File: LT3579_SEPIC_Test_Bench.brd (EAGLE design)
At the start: 300 x 300 mm, 121 parts

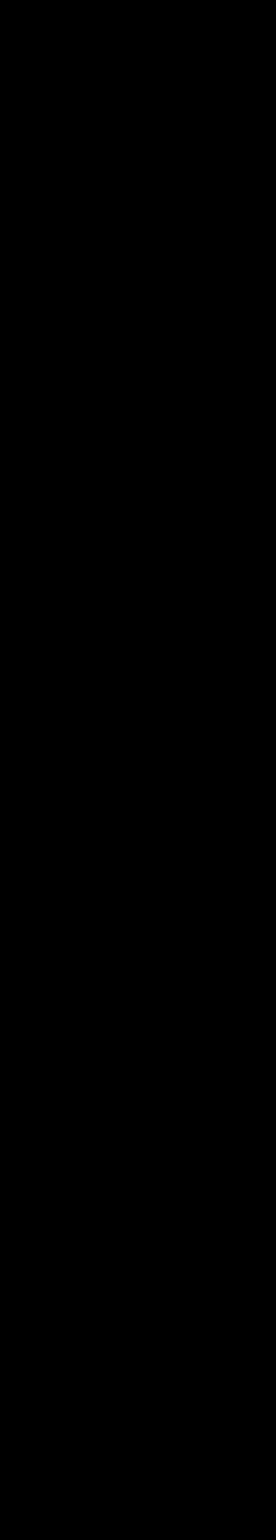
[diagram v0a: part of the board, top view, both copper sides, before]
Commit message: Added new componants to schematic and board layout
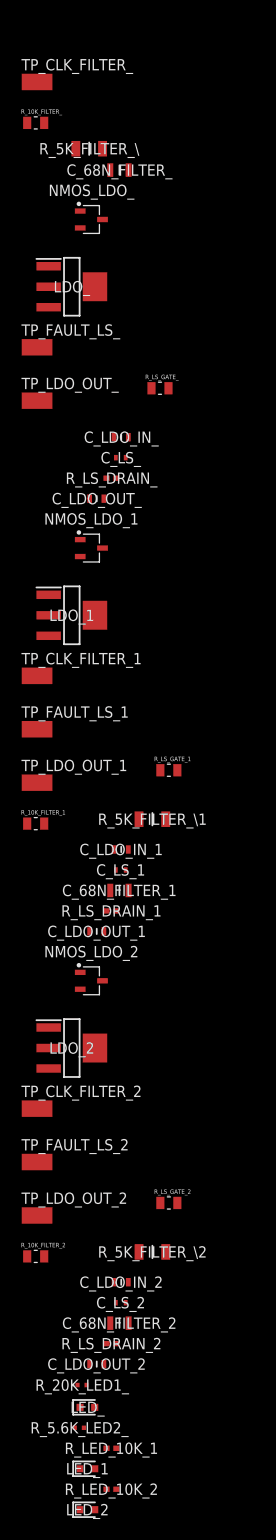
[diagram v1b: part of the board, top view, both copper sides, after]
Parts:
- added C_68N_FILTER_, C_68N_FILTER_1, C_68N_FILTER_2: CEU4J2X7R1H683K125AE, SamacSys_Parts:CAPC2013X150N
- added C_LDO_IN_, C_LDO_IN_1, C_LDO_IN_2: CGA3E1X7R1V105K080AC, SamacSys_Parts:CAPC1608X90N
- added C_LDO_OUT_, C_LDO_OUT_1, C_LDO_OUT_2: JMK107BB7475KA-T, SamacSys_Parts:CAPC1608X90N
- added C_LS_, C_LS_1, C_LS_2: CGA2B2C0G1H102J050BE, SamacSys_Parts:CAPC1005X55N
- added LDO_, LDO_1, LDO_2: LDL1117S33R, SamacSys_Parts:SOT230P700X180-4N
- added LED_, LED_1, LED_2: APTD1608LCGCK, SamacSys_Parts:APT1608CGCK
- added NMOS_LDO_, NMOS_LDO_1, NMOS_LDO_2: RTR025N05HZGTL, SamacSys_Parts:SOT95P280X110-3N
- added R_10K_FILTER_, R_10K_FILTER_1, R_10K_FILTER_2: AC0805DR-0710KL, AC0805DR-0710KL:RESC2012X60N
- added R_20K_LED1_: ERJ-2RKF2002X, SamacSys_Parts:ERJ2R_(0402)
- added R_5.6K_LED2_: ERA-2ARB562X, SamacSys_Parts:ERA2AED122X
- added R_5K_FILTER_\, R_5K_FILTER_\1, R_5K_FILTER_\2: RT1206BRD075KL, SamacSys_Parts:RESC3116X65N
- added R_LED_10K_1, R_LED_10K_2, R_LS_DRAIN_, R_LS_DRAIN_1, R_LS_DRAIN_2: MCS0402MD1002DE000, SamacSys_Parts:RESC1005X37N
- added R_LS_GATE_, R_LS_GATE_1, R_LS_GATE_2: AT0805FRE07100KL, AT0805FRE07100KL:RESC2012X60N
- added TP_CLK_FILTER_, TP_CLK_FILTER_1, TP_CLK_FILTER_2, TP_FAULT_LS_, TP_FAULT_LS_1, TP_FAULT_LS_2, TP_LDO_OUT_, TP_LDO_OUT_1, TP_LDO_OUT_2: S1751-46R, S1751-46R:S1751-46R_
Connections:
- new net CLK_FILTER_OUT_: 12P_OUTPUT_CONNECTOR1.6, C_68N_FILTER_.1, R_10K_FILTER_.2, R_5K_FILTER_\.1, TP_CLK_FILTER_.1
- new net CLK_FILTER_OUT_1: 12P_OUTPUT_CONNECTOR1.4, C_68N_FILTER_1.1, R_10K_FILTER_1.2, R_5K_FILTER_\1.1, TP_CLK_FILTER_1.1
- new net CLK_FILTER_OUT_2: 12P_OUTPUT_CONNECTOR1.2, C_68N_FILTER_2.1, R_10K_FILTER_2.2, R_5K_FILTER_\2.1, TP_CLK_FILTER_2.1
- new net FAULT_LS_OUT_: 12P_OUTPUT_CONNECTOR1.5, C_LS_.1, NMOS_LDO_.3, R_LS_DRAIN_.1, TP_FAULT_LS_.1
- new net FAULT_LS_OUT_1: 12P_OUTPUT_CONNECTOR1.3, C_LS_1.1, NMOS_LDO_1.3, R_LS_DRAIN_1.1, TP_FAULT_LS_1.1
- new net FAULT_LS_OUT_2: 12P_OUTPUT_CONNECTOR1.1, C_LS_2.1, NMOS_LDO_2.3, R_LS_DRAIN_2.1, TP_FAULT_LS_2.1
- new net LDO_OUT_: C_LDO_OUT_.1, LDO_.2, LDO_.4, R_LS_DRAIN_.2, TP_LDO_OUT_.1
- new net LDO_OUT_1: C_LDO_OUT_1.1, LDO_1.2, LDO_1.4, R_LS_DRAIN_1.2, TP_LDO_OUT_1.1
- new net LDO_OUT_2: C_LDO_OUT_2.1, LDO_2.2, LDO_2.4, R_LS_DRAIN_2.2, TP_LDO_OUT_2.1
- new net N$10: NMOS_LDO_1.1, R_LS_GATE_1.2
- new net N$11: LED_1.1, R_LED_10K_1.2
- new net N$12: R_20K_LED1_.1, R_5.6K_LED2_.1
- new net N$14: NMOS_LDO_2.1, R_LS_GATE_2.2
- new net N$15: LED_.1, R_5.6K_LED2_.2
- new net N$16: LED_2.1, R_LED_10K_2.2
- new net N$8: NMOS_LDO_.1, R_LS_GATE_.2
- net 0: now also C_68N_FILTER_.2, C_68N_FILTER_1.2, C_68N_FILTER_2.2, C_LDO_IN_.2, C_LDO_IN_1.2, C_LDO_IN_2.2, C_LDO_OUT_.2, C_LDO_OUT_1.2, C_LDO_OUT_2.2, C_LS_.2, C_LS_1.2, C_LS_2.2, LED_.2, LED_1.2, LED_2.2, NMOS_LDO_.2, NMOS_LDO_1.2, NMOS_LDO_2.2, R_5K_FILTER_\.2, R_5K_FILTER_\1.2, R_5K_FILTER_\2.2
- net CLK_: now also R_10K_FILTER_.1; no longer 12P_OUTPUT_CONNECTOR1.6
- net CLK_1: now also R_10K_FILTER_1.1; no longer 12P_OUTPUT_CONNECTOR1.4
- net CLK_2: now also R_10K_FILTER_2.1; no longer 12P_OUTPUT_CONNECTOR1.2
- net FAULT_: now also R_LS_GATE_.1; no longer 12P_OUTPUT_CONNECTOR1.5
- net FAULT_1: now also R_LS_GATE_1.1; no longer 12P_OUTPUT_CONNECTOR1.3
- net FAULT_2: now also R_LS_GATE_2.1; no longer 12P_OUTPUT_CONNECTOR1.1
- net GND: now also LDO_.1, LDO_1.1, LDO_2.1
- net VIN: now also C_LDO_IN_.1, C_LDO_IN_1.1, C_LDO_IN_2.1, LDO_.3, LDO_1.3, LDO_2.3
- net VOUT_: now also R_20K_LED1_.2
- net VOUT_1: now also R_LED_10K_1.1
- net VOUT_2: now also R_LED_10K_2.1

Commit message: Modified Board File
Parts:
- moved R_5.6K_LED2_ 269.7 mm to (123.4, 99.4), turned to 270 degrees
- moved R_20K_LED1_ 269.0 mm to (123.4, 103.5), turned to 90 degrees
- moved LED_ 265.3 mm to (120.3, 99.3), turned to 90 degrees
- moved LED_1 226.6 mm to (117.8, 39.6), turned to 270 degrees
- moved R_LED_10K_1 222.4 mm to (115.5, 41.5), turned to 270 degrees
- moved LED_2 198.6 mm to (119.9, -17.7), turned to 270 degrees
- moved R_LED_10K_2 193.7 mm to (117.5, -16.3), turned to 270 degrees
- moved TP_CLK_FILTER_1 181.0 mm to (115.1, 23.5)
- moved TP_CLK_FILTER_ 180.1 mm to (115.5, 84.5)
- moved C_68N_FILTER_1 179.9 mm to (114.5, 27.0)
- moved R_10K_FILTER_1 179.4 mm to (104.8, 33.8)
- moved R_10K_FILTER_ 178.5 mm to (110.4, 93.4)
- moved R_5K_FILTER_\ 178.3 mm to (116.2, 90.6)
- moved R_10K_FILTER_2 176.9 mm to (106.1, -25.4)
- moved C_68N_FILTER_ 174.5 mm to (115.5, 88.3)
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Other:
- board size 300 x 300 mm -> 177.6 x 301.4 mm

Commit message: Modified Board Layout
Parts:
- moved R_SHUNT_GND_2 36.8 mm to (59.4, -50.8)
- moved TP_IN_1 36.5 mm to (87.7, 7.64)
- moved TP_GND_2 36.4 mm to (61.3, -45.6)
- moved TP_CH_GND_2 35.7 mm to (57.5, -45.1)
- moved C_IN_1_2 29.9 mm to (84.1, -69.6)
- moved C_LS_2 29.9 mm to (72.3, -59.2)
- moved L1L2_2 29.9 mm to (93.7, -67.8)
- moved R_T_2 29.9 mm to (99.8, -56.9)
- moved TP_CLK_FILTER_2 29.9 mm to (102.8, -62.5)
- moved TP_FB_2 29.9 mm to (84.7, -57.9)
- moved TP_SHDN_2 29.9 mm to (105.1, -54.3)
- moved TP_SS_2 29.9 mm to (99.3, -49.2)
- moved C_1_2 29.9 mm to (89.0, -59.2)
- moved C_68N_FILTER_2 29.9 mm to (104.8, -60.1)
- moved C_F_2 29.9 mm to (83.9, -48.2)
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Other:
- board size 177.6 x 301.4 mm -> 567.8 x 300.7 mm

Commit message: Modified Board
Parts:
- moved LDO_2 142.2 mm to (7.70, 57.4)
- moved TP_RT_2 100.8 mm to (70.2, 37.1), flipped to the bottom
- moved C_F_2 98.9 mm to (35.5, 38.0)
- moved C_LDO_OUT_2 98.7 mm to (35.3, 20.5)
- moved TP_LDO_OUT_2 96.8 mm to (28.0, 22.2)
- moved R_T_2 96.8 mm to (66.2, 33.9), flipped to the bottom, turned to 180 degrees
- moved TP_FAULT_LS_2 96.3 mm to (28.1, 25.4)
- moved C_C_2 96.3 mm to (36.0, 34.3), turned to 180 degrees
- moved TP_FB_2 95.8 mm to (40.4, 27.0), flipped to the bottom, turned to 180 degrees
- moved R_C_2 95.5 mm to (40.4, 34.4), turned to 180 degrees
- moved TP_SS_2 95.1 mm to (66.2, 39.9), flipped to the bottom
- moved C_SS_2 94.9 mm to (66.0, 37.1), flipped to the bottom, turned to 180 degrees
- moved C_LDO_IN_2 93.5 mm to (40.0, 14.2)
- moved R_GATE_2 93.3 mm to (47.5, 33.8), flipped to the bottom, turned to 180 degrees
- moved TP_GATE_2 93.2 mm to (51.4, 33.7), flipped to the bottom
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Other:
- board size 567.8 x 300.7 mm -> 100 x 140 mm

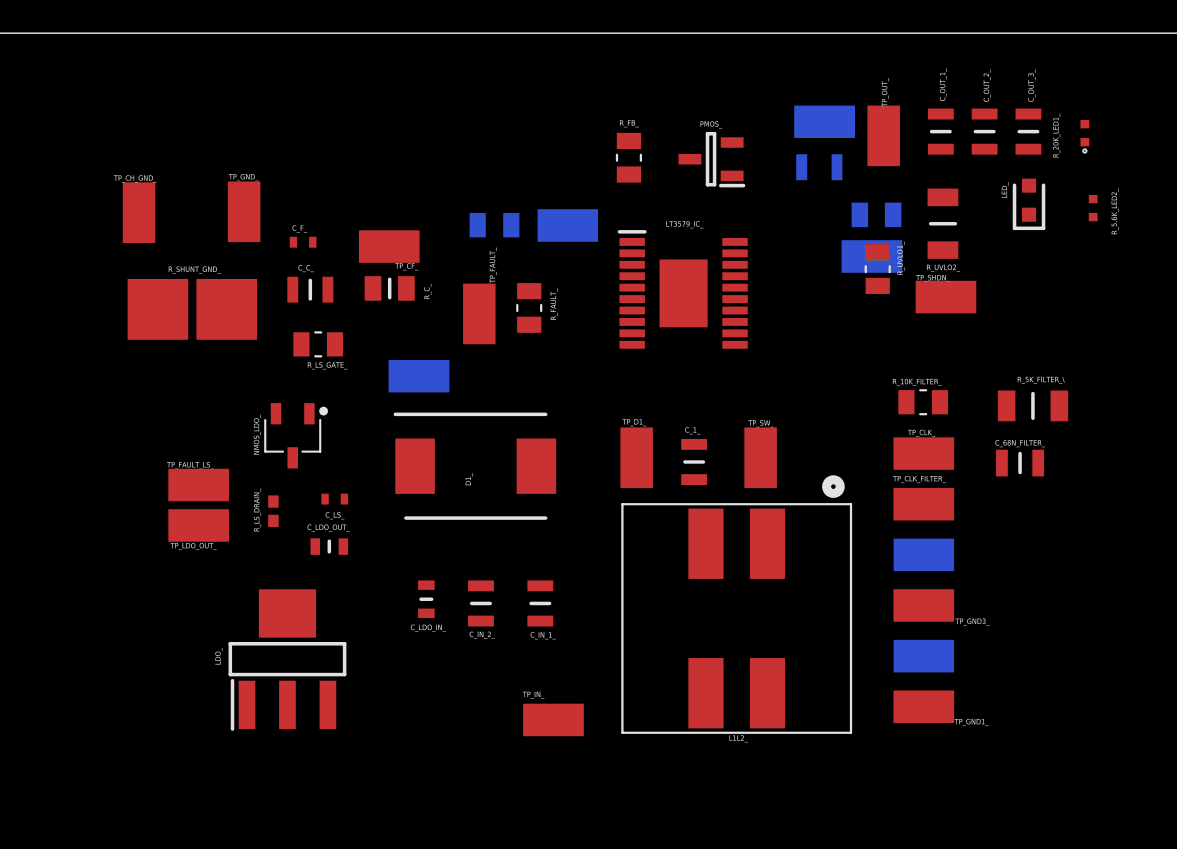
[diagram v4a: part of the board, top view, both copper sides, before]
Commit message: modified board layout
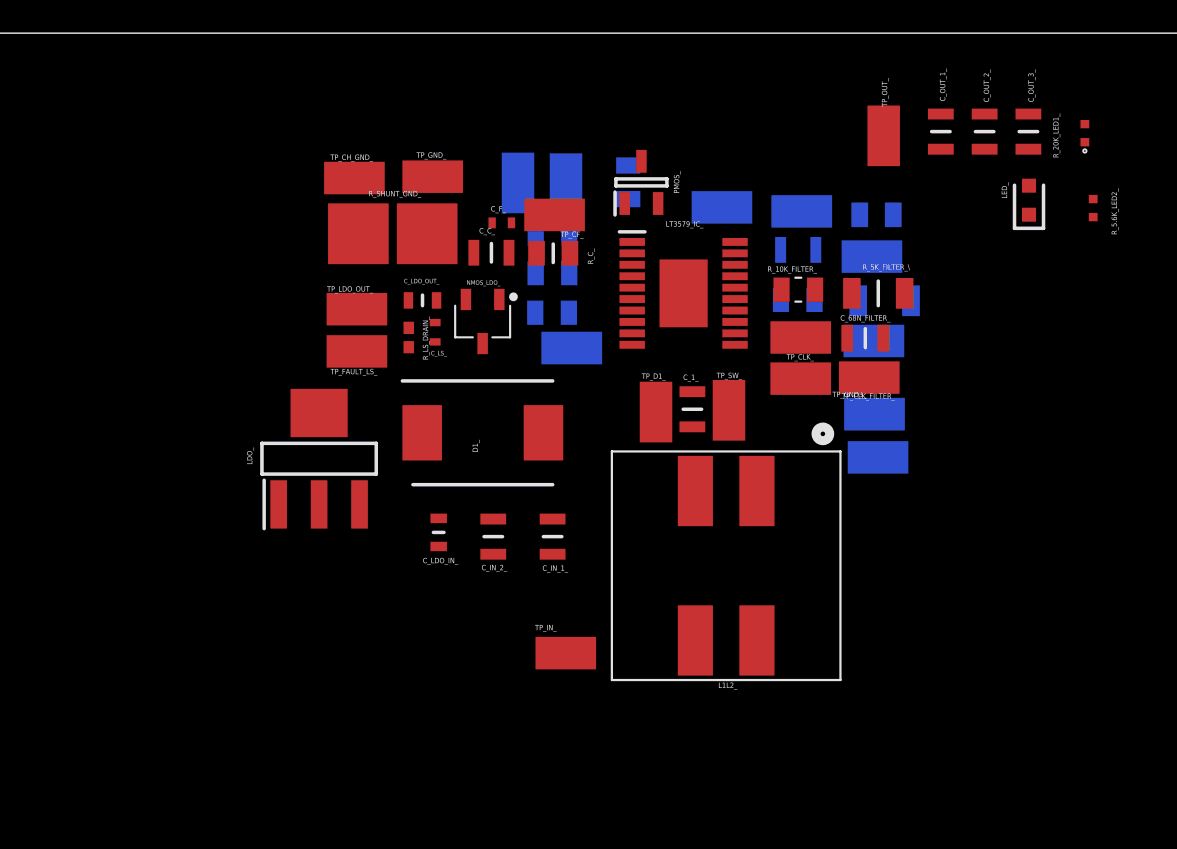
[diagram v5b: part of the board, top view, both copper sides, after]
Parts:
- moved TP_GND1_ 30.6 mm to (59.9, 130.1), flipped to the bottom
- moved TP_LDO_OUT_ 15.2 mm to (39.1, 124.3)
- moved C_LDO_OUT_ 15.0 mm to (42.9, 124.8)
- moved TP_GND3_ 14.7 mm to (64.4, 120.3)
- moved R_LS_GATE_ 13.4 mm to (50.2, 124.1), flipped to the bottom, turned to 0 degrees
- moved NMOS_LDO_ 12.6 mm to (46.3, 123.6)
- moved R_LS_DRAIN_ 12.5 mm to (42.1, 122.7), turned to 90 degrees
- moved TP_CH_GND_ 12.4 mm to (39.0, 131.8), turned to 180 degrees
- moved TP_FB_ 12.3 mm to (48.3, 131.5), turned to 270 degrees
- moved R_SHUNT_GND_ 12.2 mm to (41.2, 128.6)
- moved TP_FAULT_LS_ 11.8 mm to (39.1, 121.9)
- moved TP_GND2_ 11.6 mm to (68.8, 115.9)
- moved LDO_ 11.5 mm to (37.0, 115.8)
- moved C_F_ 11.4 mm to (47.4, 129.2)
- moved C_68N_FILTER_ 11.3 mm to (68.1, 122.7)
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
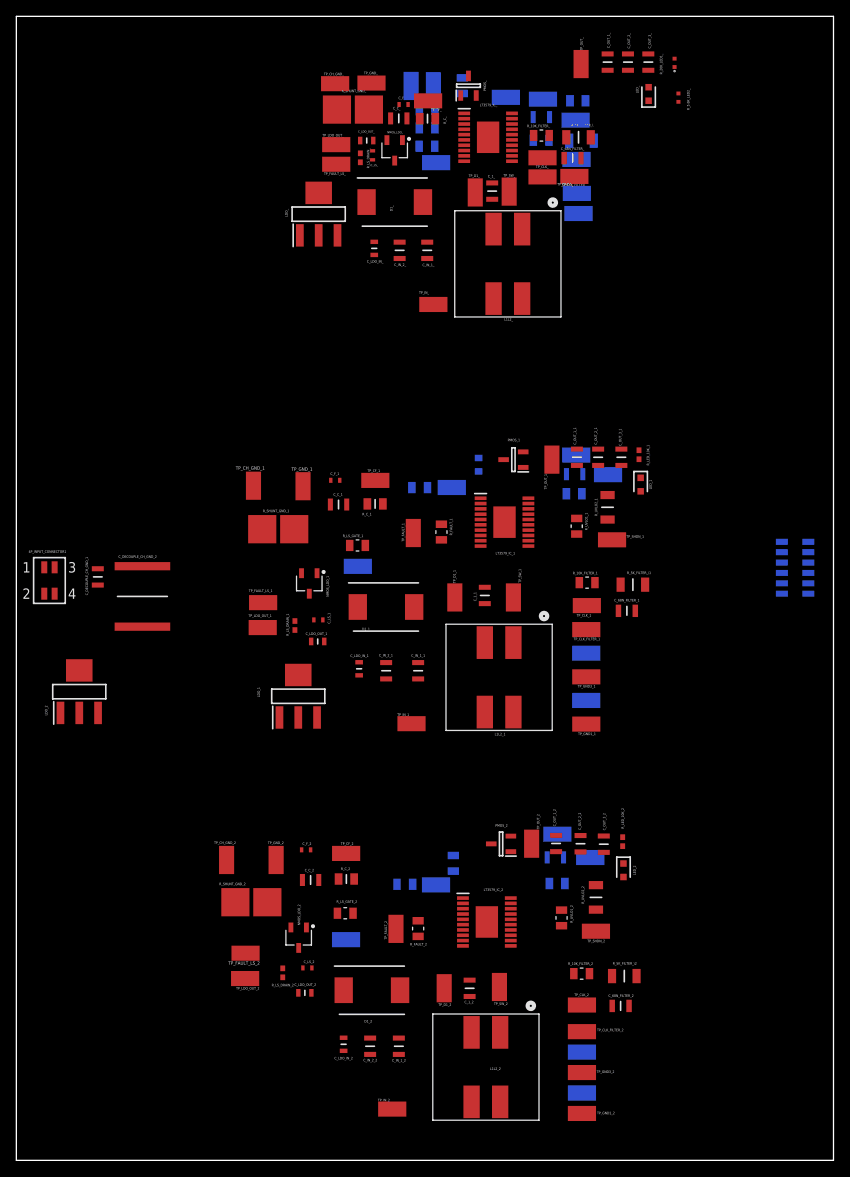
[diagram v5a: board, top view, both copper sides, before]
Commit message: Made board layout more compact. used more backside of board
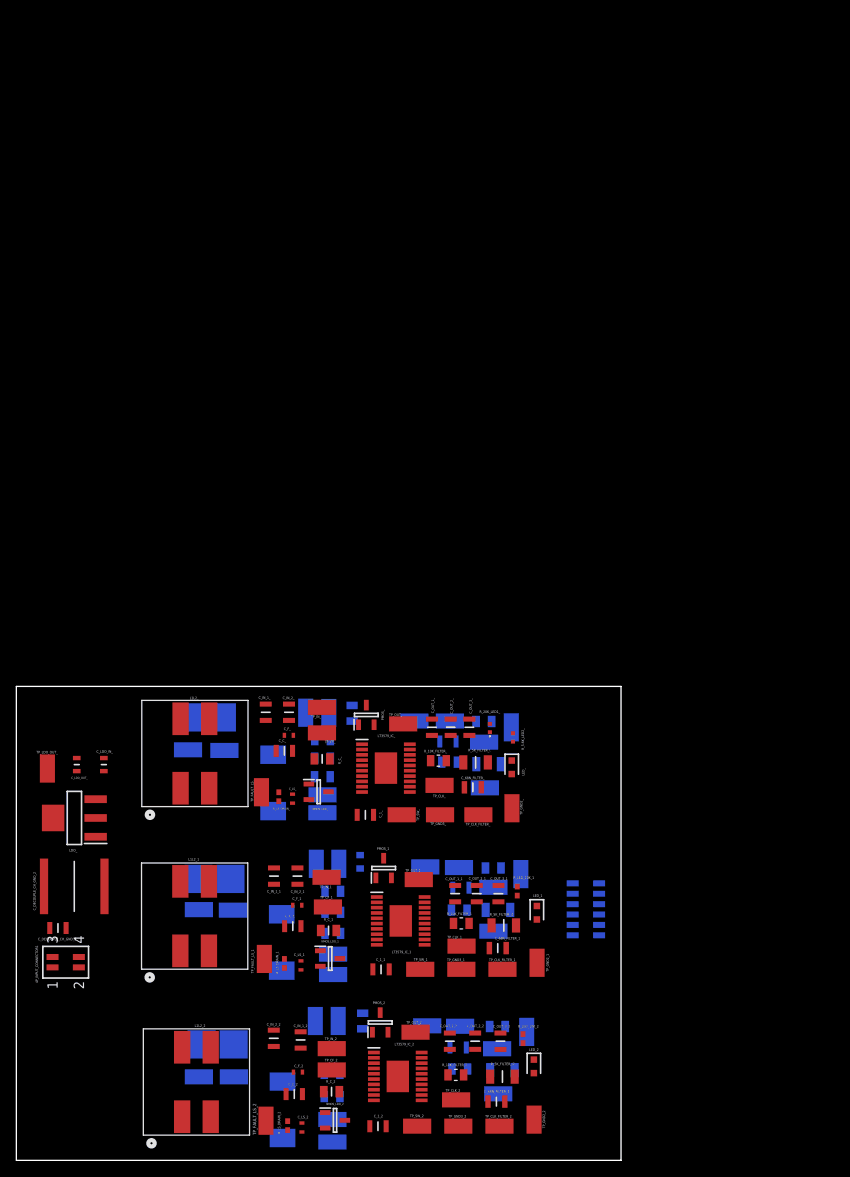
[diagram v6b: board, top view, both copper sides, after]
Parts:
- removed C_LDO_IN_1, C_LDO_IN_2: CGA3E1X7R1V105K080AC, SamacSys_Parts:CAPC1608X90N
- removed C_LDO_OUT_1, C_LDO_OUT_2: JMK107BB7475KA-T, SamacSys_Parts:CAPC1608X90N
- removed LDO_1, LDO_2: LDL1117S33R, SamacSys_Parts:SOT230P700X180-4N
- removed TP_LDO_OUT_1, TP_LDO_OUT_2: S1751-46R, S1751-46R:S1751-46R_
- NMOS_LDO_, NMOS_LDO_1, NMOS_LDO_2: value RTR025N05HZGTL -> RSR025N03HZGTL; device SamacSys_Parts:SOT95P280X110-3N -> SamacSys_Parts:SOT95P280X100-3N
- moved R_20K_LED1_ 84.5 mm to (58.0, 52.9)
- moved C_OUT_3_ 84.3 mm to (55.4, 53.0)
- moved C_OUT_2_ 84.2 mm to (53.1, 53.0)
- moved C_LDO_OUT_ 84.2 mm to (7.39, 48.4), turned to 270 degrees
- moved C_OUT_1_ 84.2 mm to (50.9, 53.0)
- moved TP_LDO_OUT_ 84.1 mm to (3.80, 48.0), turned to 90 degrees
- moved LED_ 84.1 mm to (60.6, 48.1), turned to 270 degrees
- moved TP_OUT_ 83.6 mm to (47.3, 53.4), turned to 180 degrees
- moved TP_GND_ 83.6 mm to (25.5, 50.2), flipped to the bottom, turned to 0 degrees
- moved TP_CH_GND_ 83.5 mm to (21.0, 50.2), flipped to the bottom, turned to 0 degrees
- moved R_5.6K_LED2_ 80.9 mm to (60.8, 51.8)
- moved LDO_ 79.7 mm to (7.10, 41.9), turned to 180 degrees
- moved R_C_ 79.4 mm to (37.4, 49.1)
- moved C_LS_ 79.3 mm to (33.8, 44.3)
- moved TP_GND3_ 79.1 mm to (51.9, 42.3)
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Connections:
- removed net LDO_OUT_1: C_LDO_OUT_1.1, LDO_1.2, LDO_1.4, R_LS_DRAIN_1.2, TP_LDO_OUT_1.1
- removed net LDO_OUT_2: C_LDO_OUT_2.1, LDO_2.2, LDO_2.4, R_LS_DRAIN_2.2, TP_LDO_OUT_2.1
- net 0: no longer C_LDO_IN_1.2, C_LDO_IN_2.2, C_LDO_OUT_1.2, C_LDO_OUT_2.2
- net GND: no longer LDO_1.1, LDO_2.1
- net LDO_OUT_: now also R_LS_DRAIN_1.2, R_LS_DRAIN_2.2
- net VIN: no longer C_LDO_IN_1.1, C_LDO_IN_2.1, LDO_1.3, LDO_2.3
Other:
- board size 100 x 140 mm -> 74 x 58 mm
